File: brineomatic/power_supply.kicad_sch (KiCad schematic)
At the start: 26 parts, among them J15 5.08MM, J19 5.08MM, Q6 20N06, U2 LM74700, U5 XL1509-5.0

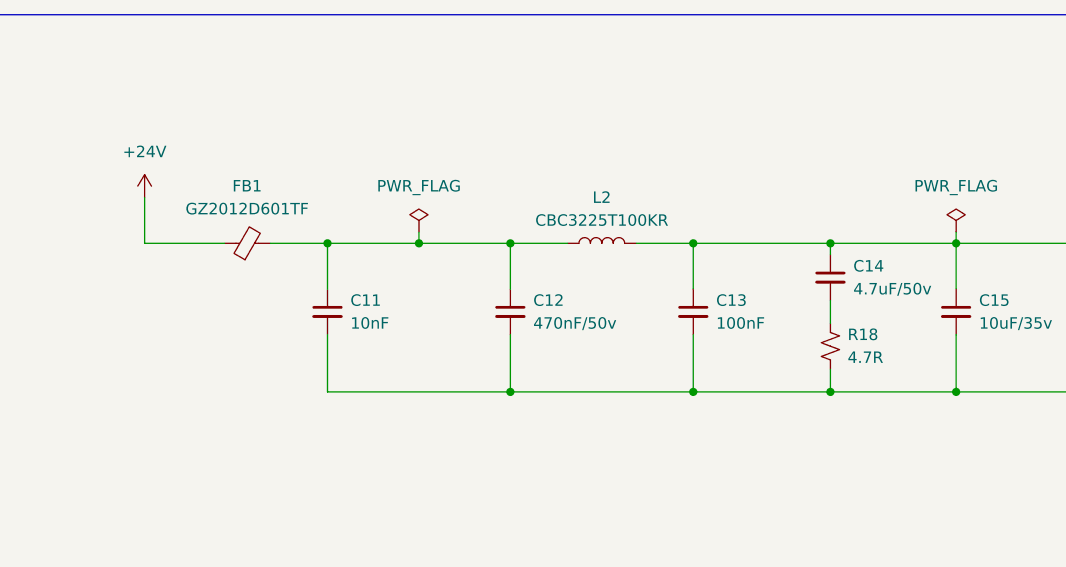
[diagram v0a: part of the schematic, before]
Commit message: switched to onboard esp32-s3 and re-drew tmc2209 driver
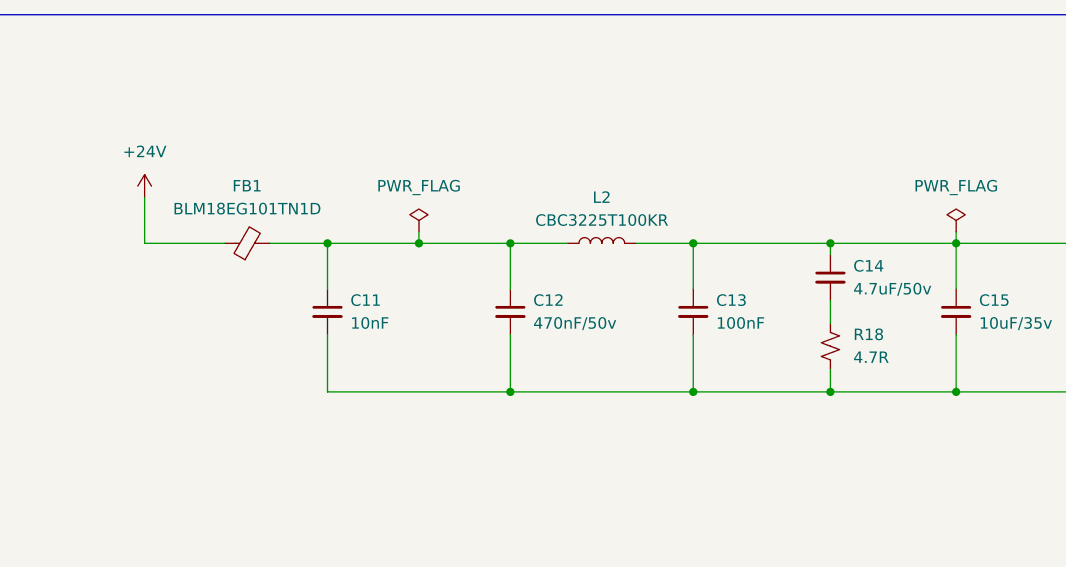
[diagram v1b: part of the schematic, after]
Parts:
- FB1: value GZ2012D601TF -> BLM18EG101TN1D; footprint Inductor_SMD:L_0805_2012Metric -> Inductor_SMD:L_0603_1608Metric; LCSC C1017 -> C76893
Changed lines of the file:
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@@
 		(fields_autoplaced yes)
 		(property "Reference" "R18"
-			(at 130.175 130.81 0)
+			(at 130.81 130.8099 0)
 			(effects
 				(font
@@
 		)
 		(property "Value" "4.7R"
-			(at 130.175 133.35 0)
+			(at 130.81 133.3499 0)
 			(effects
 				(font
@@
 			)
 		)
-		(property "Description" ""
+		(property "Description" "Resistor, small US symbol"
 			(at 128.27 132.08 0)
 			(effects
@@
 			)
 		)
-		(property "Value" "GZ2012D601TF"
+		(property "Value" "BLM18EG101TN1D"
 			(at 63.4619 116.84 90)
 			(effects
@@
 			)
 		)
-		(property "Footprint" "Inductor_SMD:L_0805_2012Metric"
+		(property "Footprint" "Inductor_SMD:L_0603_1608Metric"
 			(at 63.5 122.428 90)
 			(effects
@@
 			)
 		)
-		(property "LCSC" "C1017"
+		(property "LCSC" "C76893"
 			(at 63.5 120.65 90)
 			(effects

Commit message: tmc2209 driver schematic checked and laid out nicely.
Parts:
- renumbered C14 to C10, C15 to C11, C16 to C12, C11 to C6, C4 to C7, C12 to C8, C13 to C9, D19 to D10, D9 to D11, D3 to D8, D8 to D9, F4 to F2, J19 to J8, J15 to J9, L2 to L1, L3 to L2, Q6 to Q3, R21 to R19, R32 to R20, U5 to U3

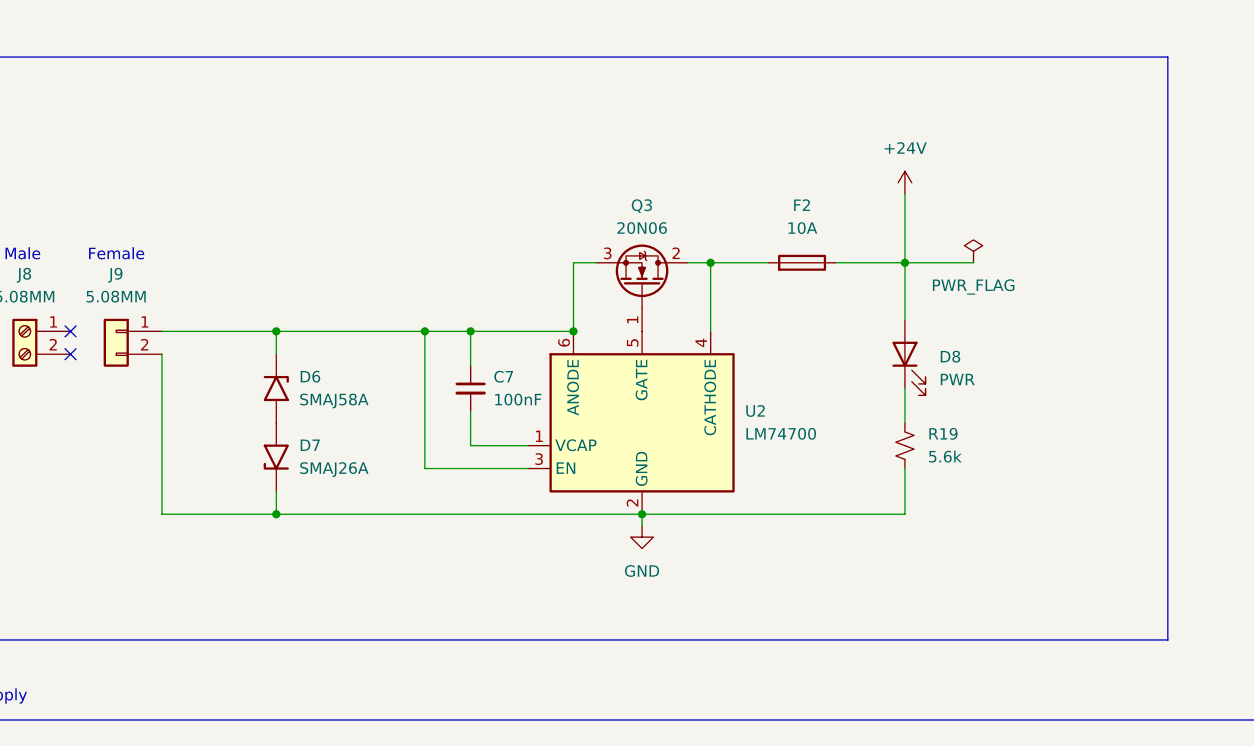
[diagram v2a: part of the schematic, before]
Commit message: single 5v supply works just fine
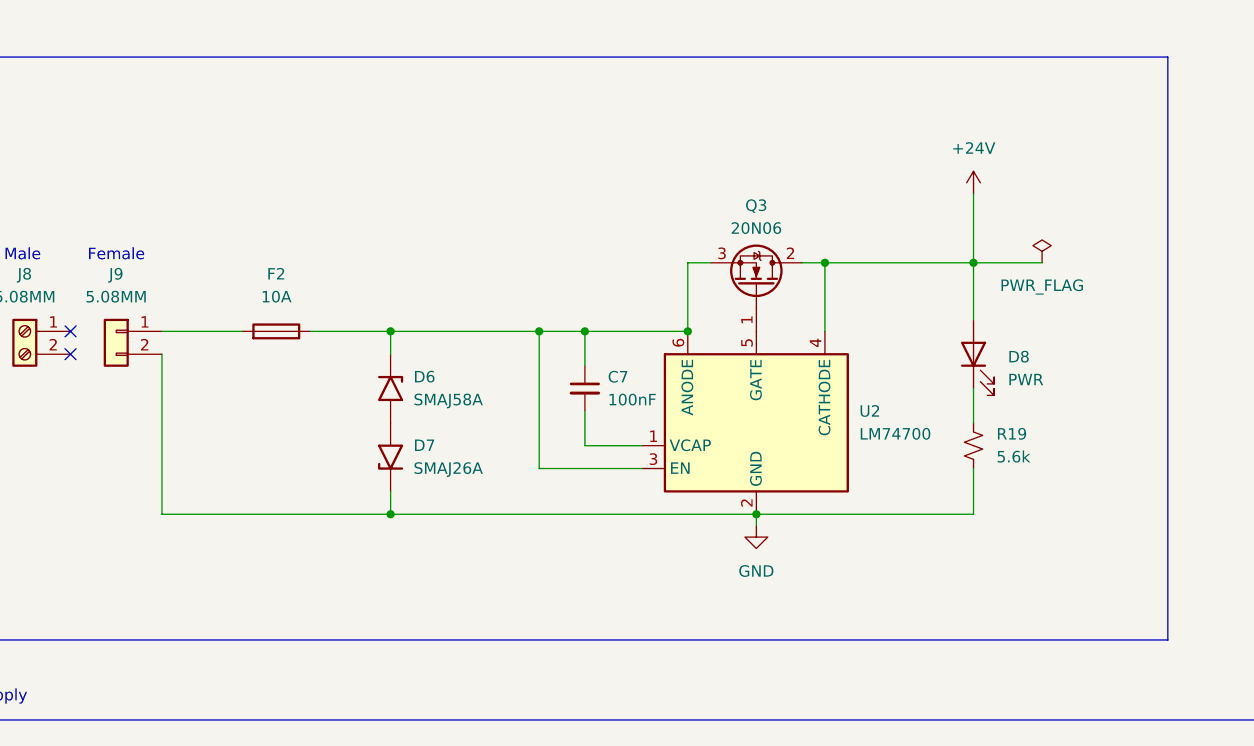
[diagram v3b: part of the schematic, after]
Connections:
- net +24V: now also Q3.2 (D), U2.4 (CATHODE); no longer F2.1
- net at C7.1, D6.1 (A1), Q3.3 (S)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: now also F2.1; no longer J9.1 (Pin_1)
- new net: F2.2, J9.1 (Pin_1)
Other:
- moved on the sheet: C7, D6, D7, D8, F2, Q3, R19, U2

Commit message: all the important parts have 3d models now.
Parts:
- F3: footprint Fuse:Fuse_1812_4532Metric_Pad1.30x3.40mm_HandSolder -> yarrboard:Fuse_1812_4532Metric
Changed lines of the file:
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@@
 			)
 		)
-		(property "Footprint" "Fuse:Fuse_1812_4532Metric_Pad1.30x3.40mm_HandSolder"
+		(property "Footprint" "yarrboard:Fuse_1812_4532Metric"
 			(at 204.47 121.92 0)
 			(effects

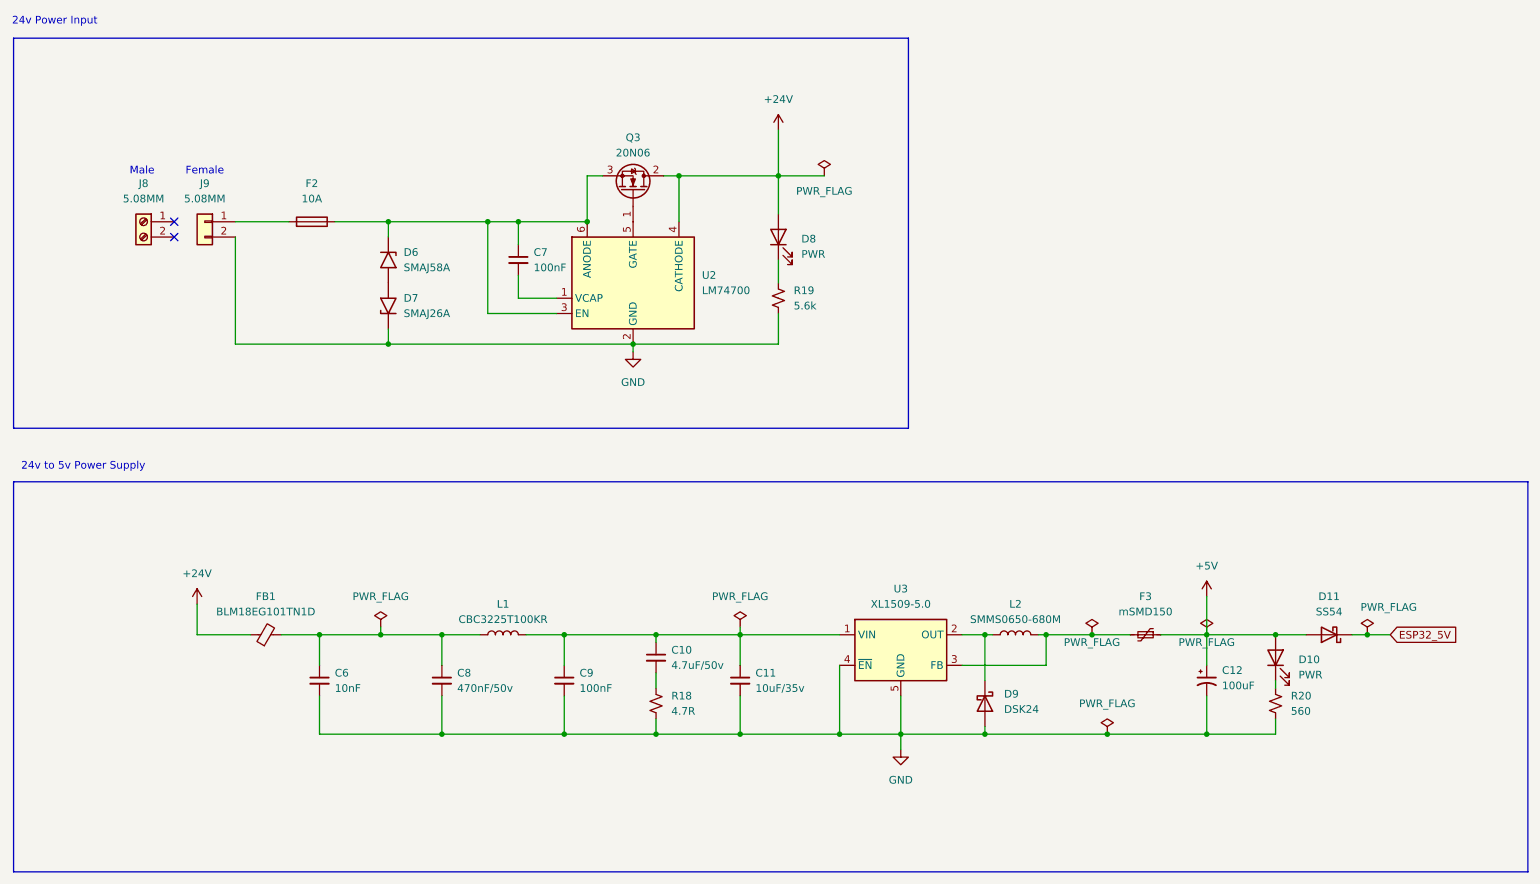
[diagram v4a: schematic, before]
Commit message: aligned all connectors with board edge
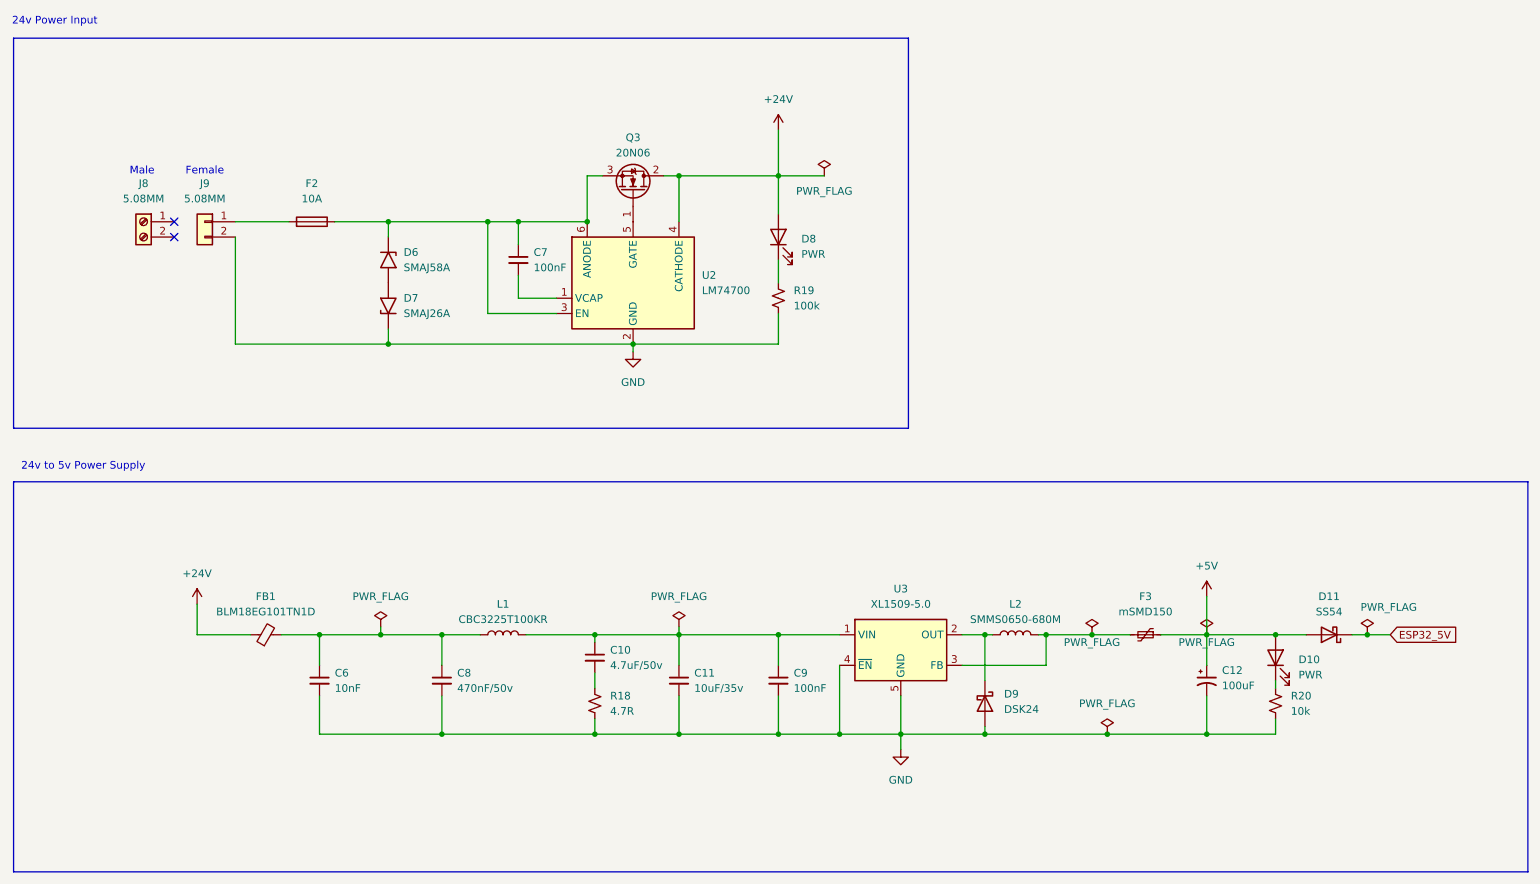
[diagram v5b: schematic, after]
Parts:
- R19: value 5.6k -> 100k
- R20: value 560 -> 10k
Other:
- moved on the sheet: C10, C11, C9, R18

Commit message: fully routed and erc/drc passed
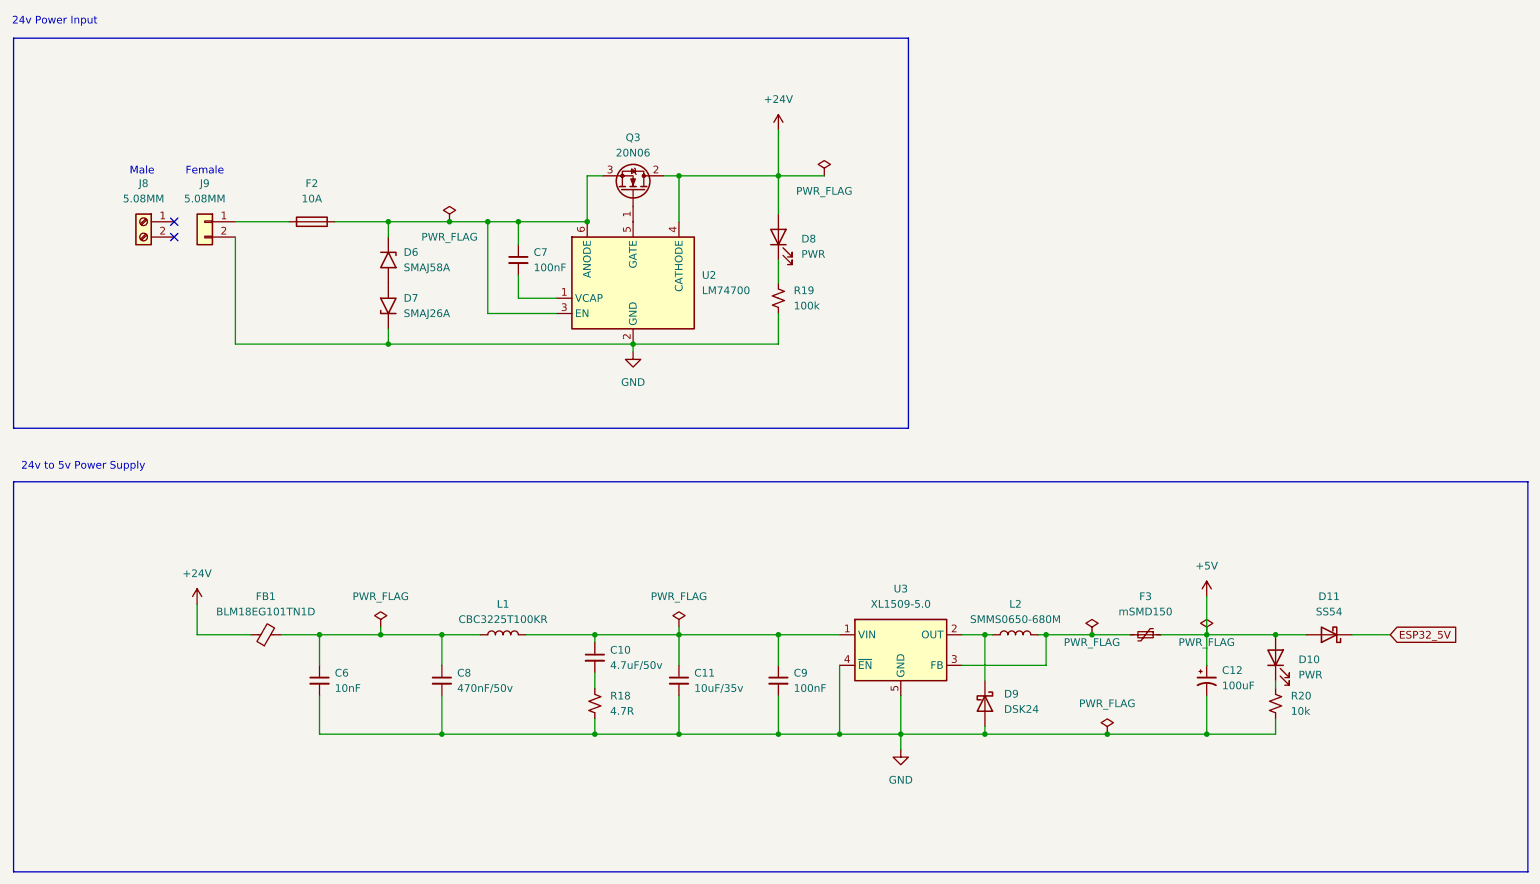
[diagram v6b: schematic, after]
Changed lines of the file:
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@@
 	)
 	(junction
-		(at 105.41 52.07)
+		(at 93.98 52.07)
 		(diameter 0)
 		(color 0 0 0 0)
 	)
 	(junction
-		(at 246.38 120.65)
+		(at 105.41 52.07)
 		(diameter 0)
 		(color 0 0 0 0)
@@
 	(wire
 		(pts
-			(xy 246.38 120.65) (xy 250.19 120.65)
+			(xy 243.84 120.65) (xy 250.19 120.65)
 		)
 		(stroke
@@
 	(wire
 		(pts
+			(xy 93.98 52.07) (xy 100.33 52.07)
+		)
+		(stroke
+			(width 0)
+			(type default)
+		)
+	)
+	(wire
+		(pts
 			(xy 124.46 72.39) (xy 124.46 73.66)
 		)
@@
 	(wire
 		(pts
-			(xy 83.82 52.07) (xy 100.33 52.07)
+			(xy 83.82 52.07) (xy 93.98 52.07)
 		)
 		(stroke
@@
 	(wire
 		(pts
-			(xy 243.84 120.65) (xy 246.38 120.65)
-		)
-		(stroke
-			(width 0)
-			(type default)
-		)
-	)
-	(wire
-		(pts
 			(xy 132.08 120.65) (xy 148.59 120.65)
 		)
@@
 	(symbol
 		(lib_id "power:PWR_FLAG")
-		(at 246.38 120.65 0)
-		(unit 1)
-		(exclude_from_sim no)
-		(in_bom yes)
-		(on_board yes)
-		(dnp no)
-		(property "Reference" "#FLG09"
-			(at 246.38 118.745 0)
-			(effects
-				(font
-					(size 1.27 1.27)
-				)
-				(hide yes)
-			)
-		)
-		(property "Value" "PWR_FLAG"
-			(at 249.936 116.078 0)
-			(effects
-				(font
-					(size 1.27 1.27)
-				)
-			)
-		)
-		(property "Footprint" ""
-			(at 246.38 120.65 0)
-			(effects
-				(font
-					(size 1.27 1.27)
-				)
-				(hide yes)
-			)
-		)
-		(property "Datasheet" "~"
-			(at 246.38 120.65 0)
-			(effects
-				(font
-					(size 1.27 1.27)
-				)
-				(hide yes)
-			)
-		)
-		(property "Description" "Special symbol for telling ERC where power comes from"
-			(at 246.38 120.65 0)
-			(effects
-				(font
-					(size 1.27 1.27)
-				)
-				(hide yes)
-			)
-		)
-		(pin "1"
-		)
-		(instances
-			(project "brineomatic"
-				(path "/96477ae2-ef08-48f3-8dd4-fe4478541f68/7cbb3b3c-cf93-4880-b816-c6df902b993c"
-					(reference "#FLG09")
-					(unit 1)
-				)
-			)
-		)
-	)
-	(symbol
-		(lib_id "power:PWR_FLAG")
 		(at 156.21 44.45 0)
 		(unit 1)
@@
 					(unit 1)
 				)
+			)
+		)
+	)
+	(symbol
+		(lib_id "power:PWR_FLAG")
+		(at 93.98 52.07 0)
+		(unit 1)
+		(exclude_from_sim no)
+		(in_bom yes)
+		(on_board yes)
+		(dnp no)
+		(property "Reference" "#FLG01"
+			(at 93.98 50.165 0)
+			(effects
+				(font
+					(size 1.27 1.27)
+				)
+				(hide yes)
+			)
+		)
+		(property "Value" "PWR_FLAG"
+			(at 93.98 54.61 0)
+			(effects
+				(font
+					(size 1.27 1.27)
+				)
+			)
+		)
+		(property "Footprint" ""
+			(at 93.98 52.07 0)
+			(effects
+				(font
+					(size 1.27 1.27)
+				)
+				(hide yes)
+			)
+		)
+		(property "Datasheet" "~"
+			(at 93.98 52.07 0)
+			(effects
+				(font
+					(size 1.27 1.27)
+				)
+				(hide yes)
+			)
+		)
+		(property "Description" "Special symbol for telling ERC where power comes from"
+			(at 93.98 52.07 0)
+			(effects
+				(font
+					(size 1.27 1.27)
+				)
+				(hide yes)
+			)
+		)
+		(pin "1"
+		)
+		(instances
+			(project "brineomatic"
+				(path "/96477ae2-ef08-48f3-8dd4-fe4478541f68/7cbb3b3c-cf93-4880-b816-c6df902b993c"
+					(reference "#FLG01")
+					(unit 1)
+				)
